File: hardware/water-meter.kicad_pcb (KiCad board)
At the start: 2 copper layers, 58 x 51.1 mm, 19 parts, among them J1 Conn_01x04, Q1 L-93DP3BT, U1 LM393

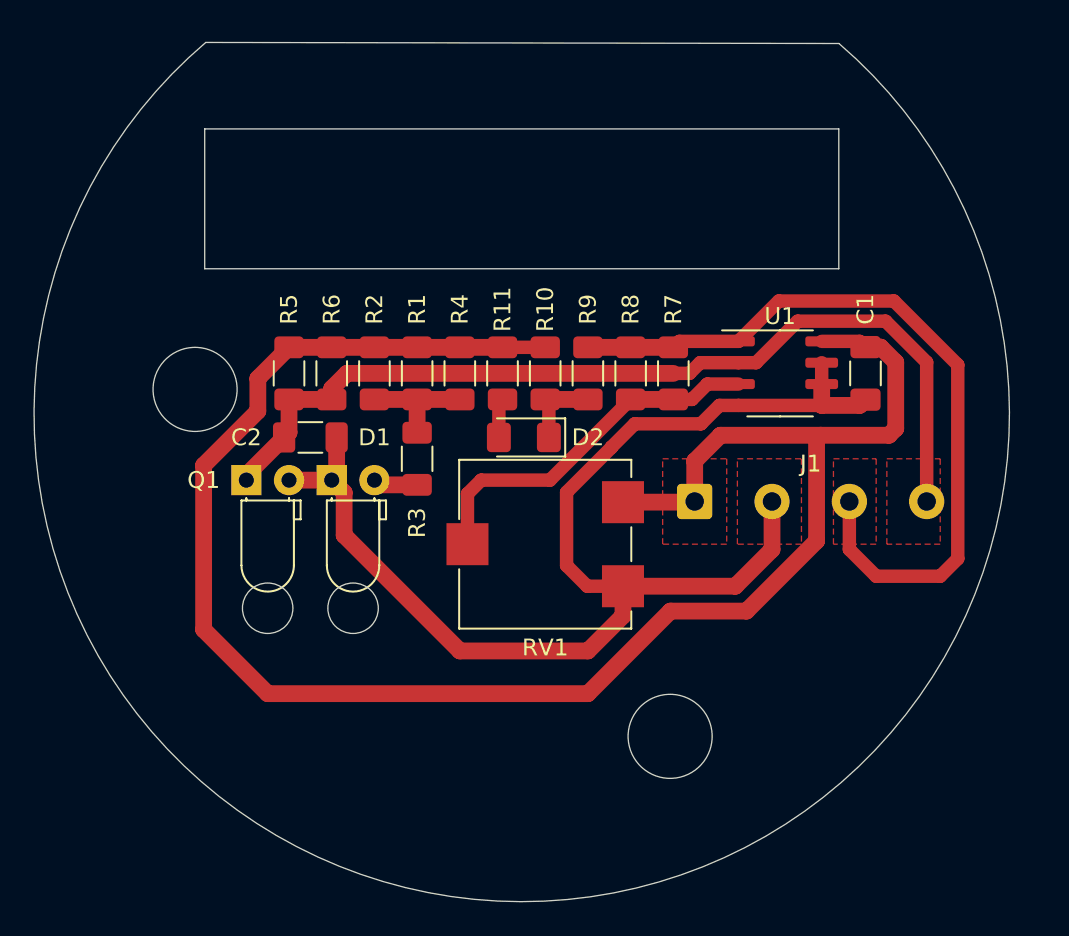
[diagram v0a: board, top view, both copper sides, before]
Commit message: Fix hardware design flaws
... hopefully. I didn't mill a new board. Instead, I just drilled larger
holes and sanded the edge a bit.
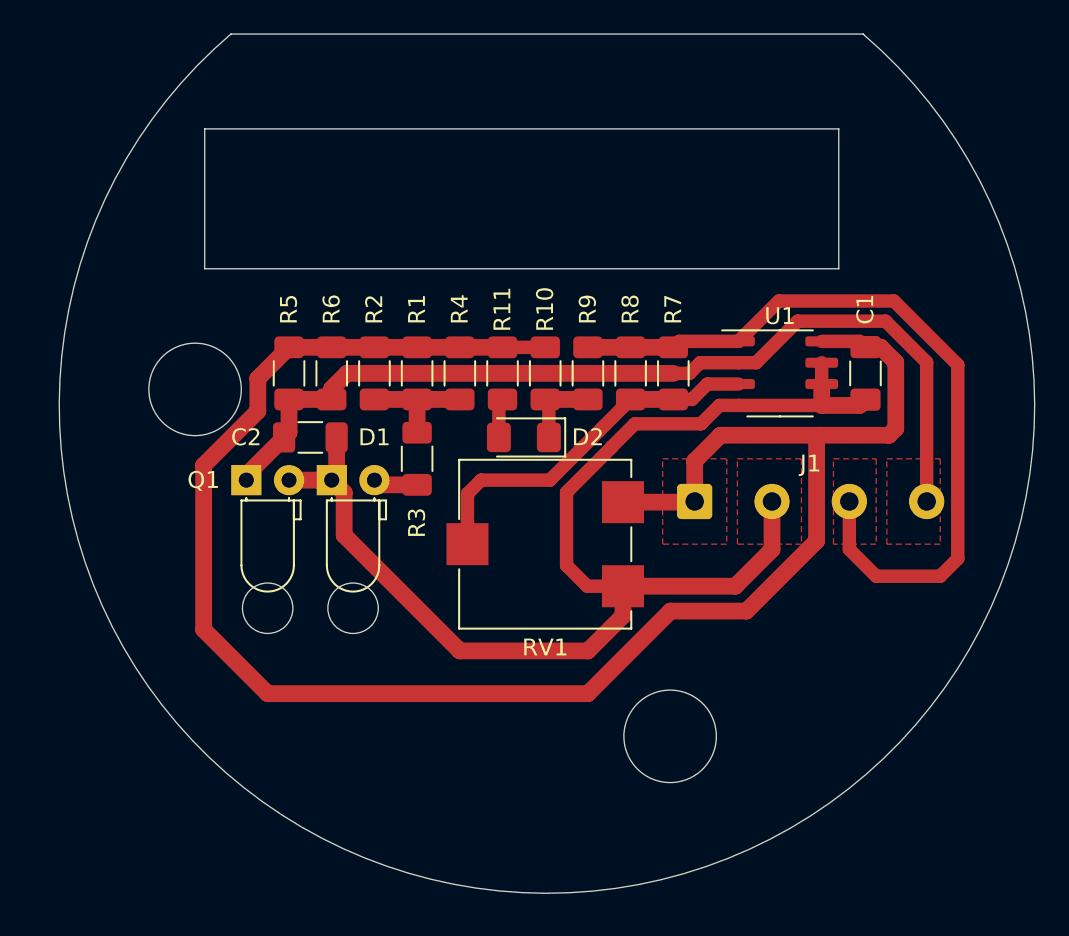
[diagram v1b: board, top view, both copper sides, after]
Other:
- outline, holes or cut-outs redrawn
- board text removed: "TODO the lower left edge is too close 5 mm holes are too tight, redrilled to 5,5 mm"
